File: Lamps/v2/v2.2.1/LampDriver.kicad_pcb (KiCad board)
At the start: 2 copper layers, 50 x 42.8 mm, 25 parts, among them J1 JST XH 1x4, J2 Screw_Terminal_01x02, J3 1x6 MOLEX KK 396, Q1 BSS138, Q2 BSS138, Q3 BSS138, Q4 FDD4141, Q5 FDD4141, Q6 FDD4141

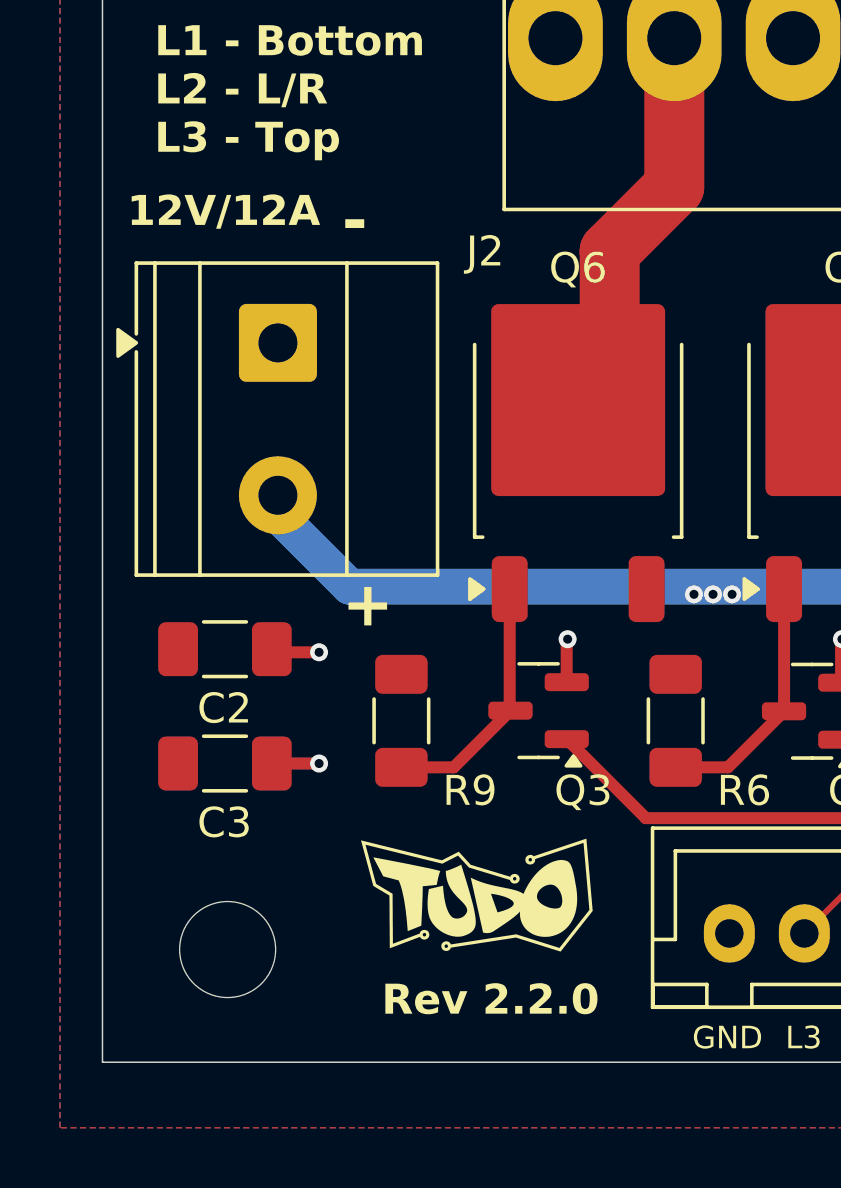
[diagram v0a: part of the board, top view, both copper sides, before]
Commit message: Lamps: PCB: minor changes qualify as v2.2.1
Signed-off-by: Patrick Pedersen <ctx.xda@gmail.com>
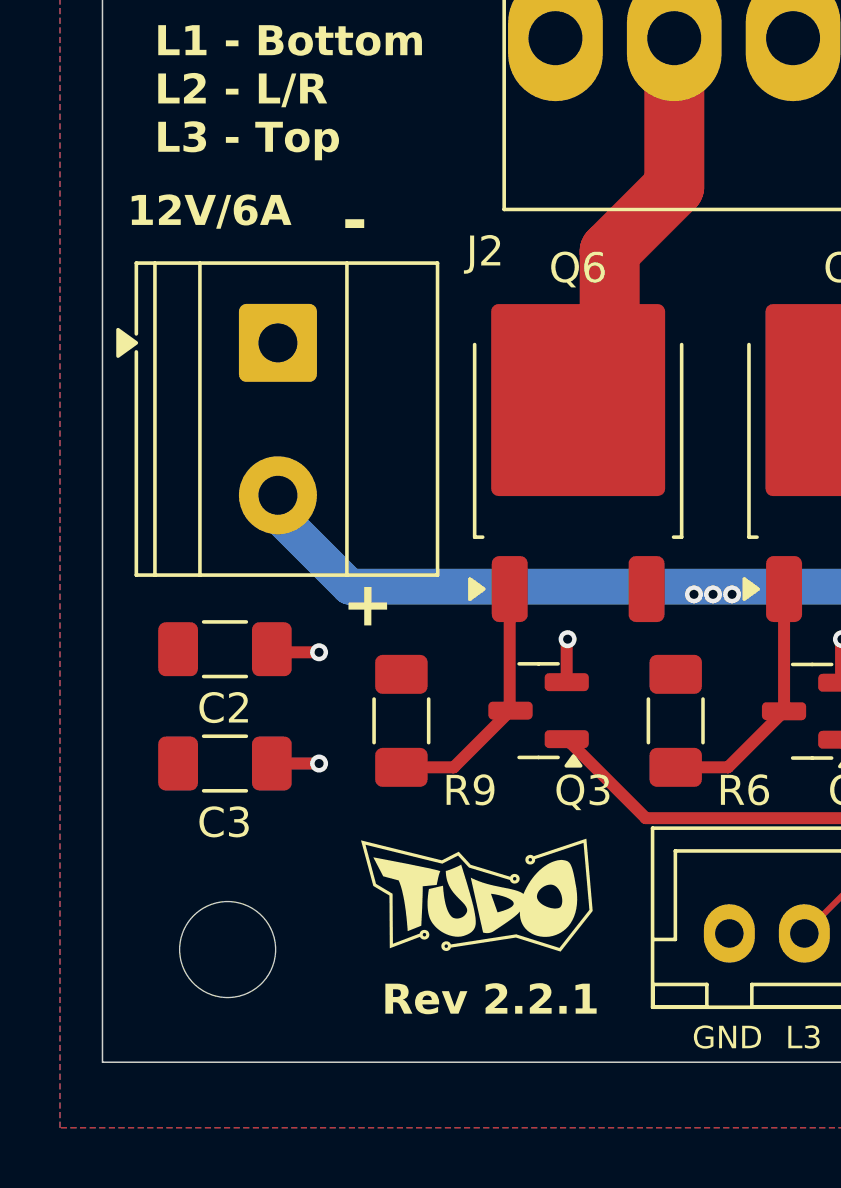
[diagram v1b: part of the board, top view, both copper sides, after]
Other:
- board text added: "12V/6A"
- board text added: "Rev 2.2.1"
- board text removed: "12V/12A"
- board text removed: "Rev 2.2.0"
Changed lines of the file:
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@@
 		)
 	)
-	(gr_text "Rev 2.2.0"
+	(gr_text "Rev 2.2.1"
 		(at 90.7288 80.139801 0)
 		(layer "F.SilkS")
@@
 		)
 	)
-	(gr_text "12V/12A"
+	(gr_text "12V/6A"
 		(at 82.2452 53.848 0)
 		(layer "F.SilkS")
